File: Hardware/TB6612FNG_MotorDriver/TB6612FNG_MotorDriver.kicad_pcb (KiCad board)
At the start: 4 copper layers, 34 x 34 mm, 12 parts, among them J1 01x04, J2 01x04, J3 01x05, J4 01x02, U1 TB6612FNG

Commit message: Hardware updates and cleanup
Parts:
- C1, C2: footprint Capacitor_SMD:C_0805_2012Metric_Pad1.18x1.45mm_HandSolder -> General:0805_HS
- J1, J2: value 01x04 -> Conn_01x04
- J3: value 01x05 -> Conn_01x05
- J4: value 01x02 -> Conn_01x02
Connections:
- net +12V renamed Net-(J3-Pin_1)
- net +3.3V renamed Net-(J3-Pin_5)
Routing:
- net Net-(J1-Pin_4): track 0.00 -> 20.6 mm
- net Net-(J4-Pin_1): track 0.00 -> 20.5 mm, vias 0 -> 1
- net Net-(J1-Pin_3): track 0.00 -> 20.2 mm
- net Net-(J3-Pin_1): track 13.0 -> 33.0 mm, vias 12 -> 2
- net Net-(J1-Pin_2): track 0.00 -> 17.8 mm
- net Net-(J1-Pin_1): track 0.00 -> 17.5 mm
- net Net-(J4-Pin_2): track 0.00 -> 13.3 mm
- net Net-(J3-Pin_5): track 6.20 -> 15.8 mm, vias 3 -> 0
- net GND: track 20.3 -> 12.9 mm, vias 16 -> 6
- removed copper zone on F.Cu, net GND
- removed copper zone on In1.Cu, net GND
- removed copper zone on In2.Cu, net Net-(J3-Pin_1)
- removed copper zone on In2.Cu, net Net-(J3-Pin_5)
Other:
- copper layers 4 -> 2
- board text removed: "TB6612FNG Motor Driver rev. B"

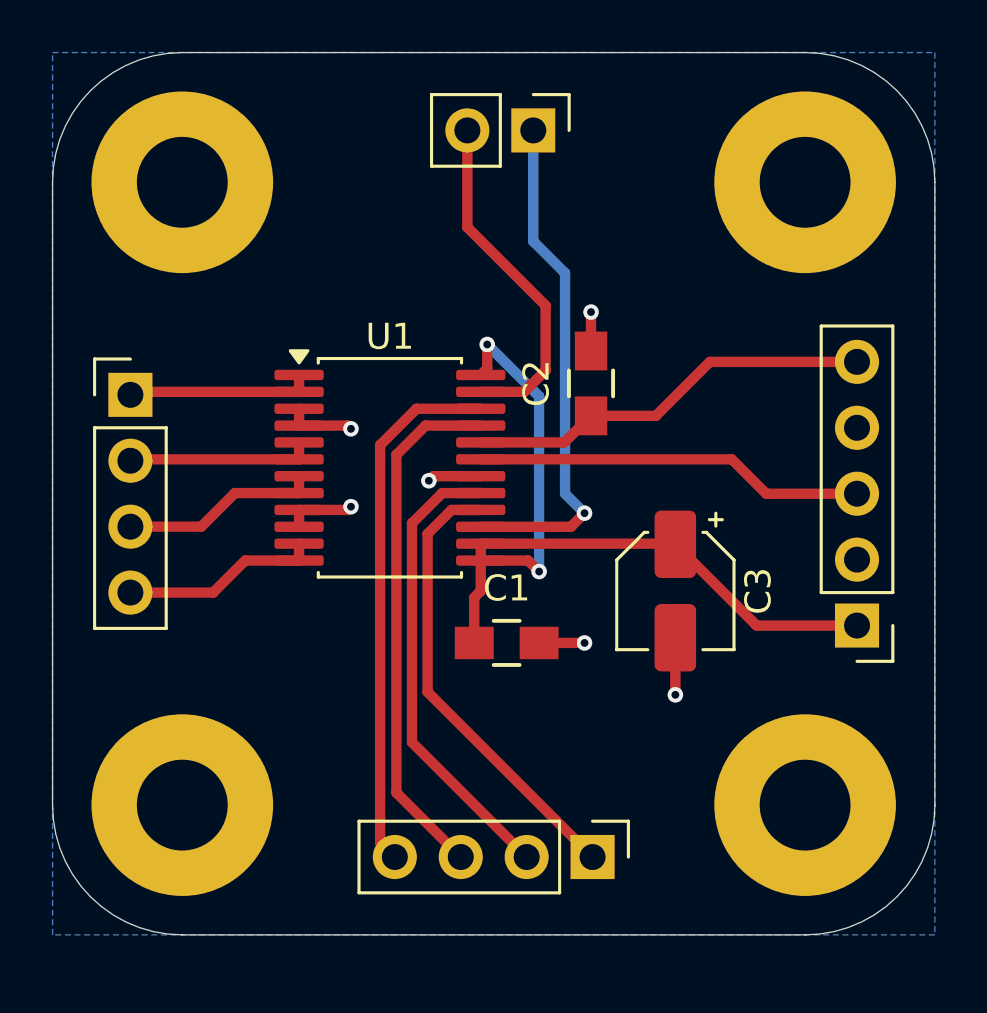
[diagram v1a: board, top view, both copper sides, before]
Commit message: Hardware updates. Add Lr04 lora module datasheets
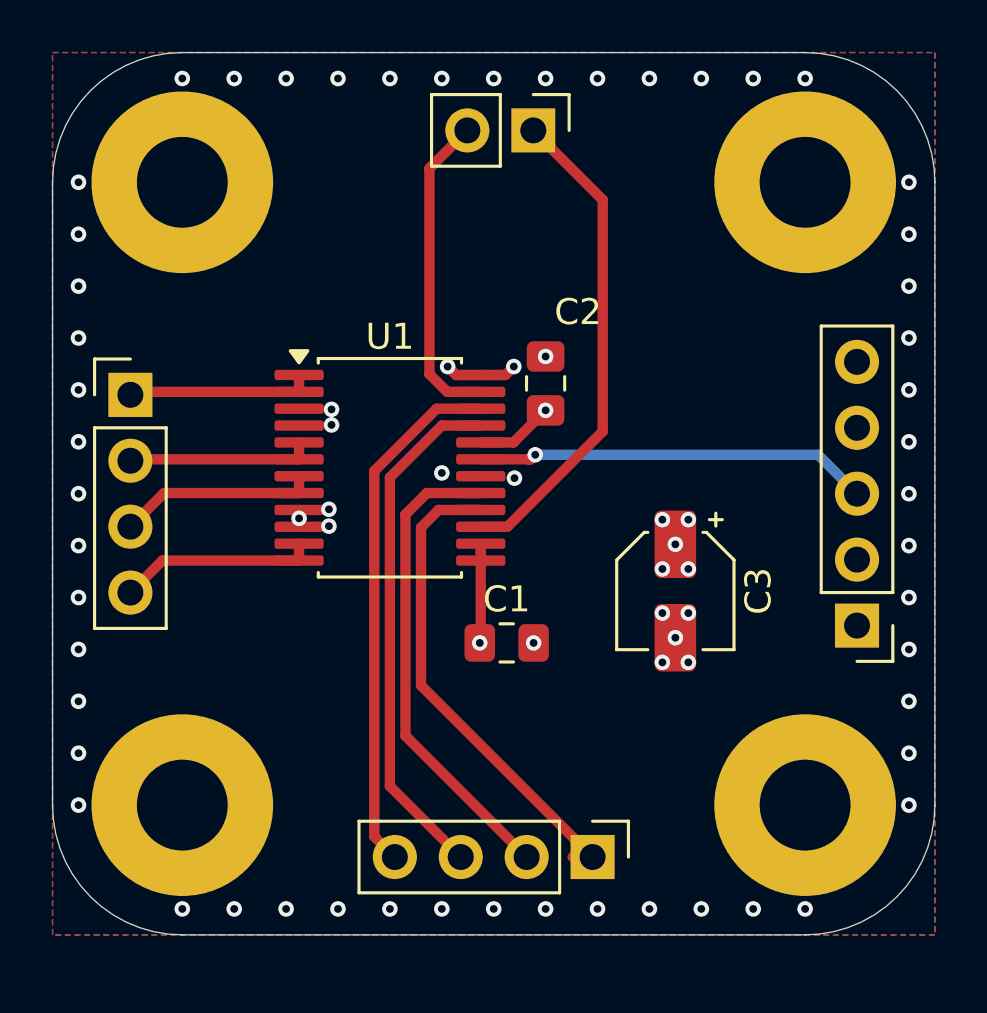
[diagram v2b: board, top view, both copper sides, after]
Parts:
- C1, C2: footprint General:0805_HS -> Capacitor_SMD:C_0805_2012Metric_Pad1.18x1.45mm_HandSolder
- moved C2 1.75 mm to (94.0, 87.8)
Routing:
- net Net-(J3-Pin_1): track 33.0 -> 6.66 mm, vias 2 -> 8
- net GND: track 12.9 -> 0.00 mm, vias 6 -> 66
- net Net-(J3-Pin_5): track 15.8 -> 3.01 mm, vias 0 -> 1
- net Net-(J4-Pin_1): track 20.5 -> 18.9 mm, vias 1 -> 0
- net Net-(J1-Pin_1): track 17.5 -> 18.8 mm
- net Net-(J4-Pin_2): track 13.3 -> 12.3 mm
- net Net-(J1-Pin_2): track 17.8 -> 18.4 mm
- net Net-(J3-Pin_3): track 15.0 -> 15.2 mm, vias 0 -> 1
- added copper zone on F.Cu, net GND
- added copper zone on In1.Cu, net GND
- added copper zone on In2.Cu, net GND
- added copper zone on In2.Cu, net Net-(J3-Pin_1)
- added copper zone on In2.Cu, net Net-(J3-Pin_5)
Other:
- copper layers 2 -> 4
- board text added: "TB6612FNG Motor Driver rev. B"
